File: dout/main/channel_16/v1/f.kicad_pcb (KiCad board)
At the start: 2 copper layers, 76.8 x 81.3 mm, 25 parts, among them J1 fm16_i, J10 dio_channel_i, J11 dio_channel_i, J12 dio_channel_i, J13 dio_channel_i, J14 dio_channel_i, J15 dio_channel_i, J16 dio_channel_i, J17 dio_channel_i, J18 data_manager_i, J19 data_manager_i, J2 dio_channel_i, J20 wrs_i, J21 wrs_i, J22 S0, J23 S1, J24 bus_i, J25 selector4_i, J3 dio_channel_i, J4 dio_channel_i, J5 dio_channel_i, J6 dio_channel_i, J7 dio_channel_i, J8 dio_channel_i, J9 dio_channel_i

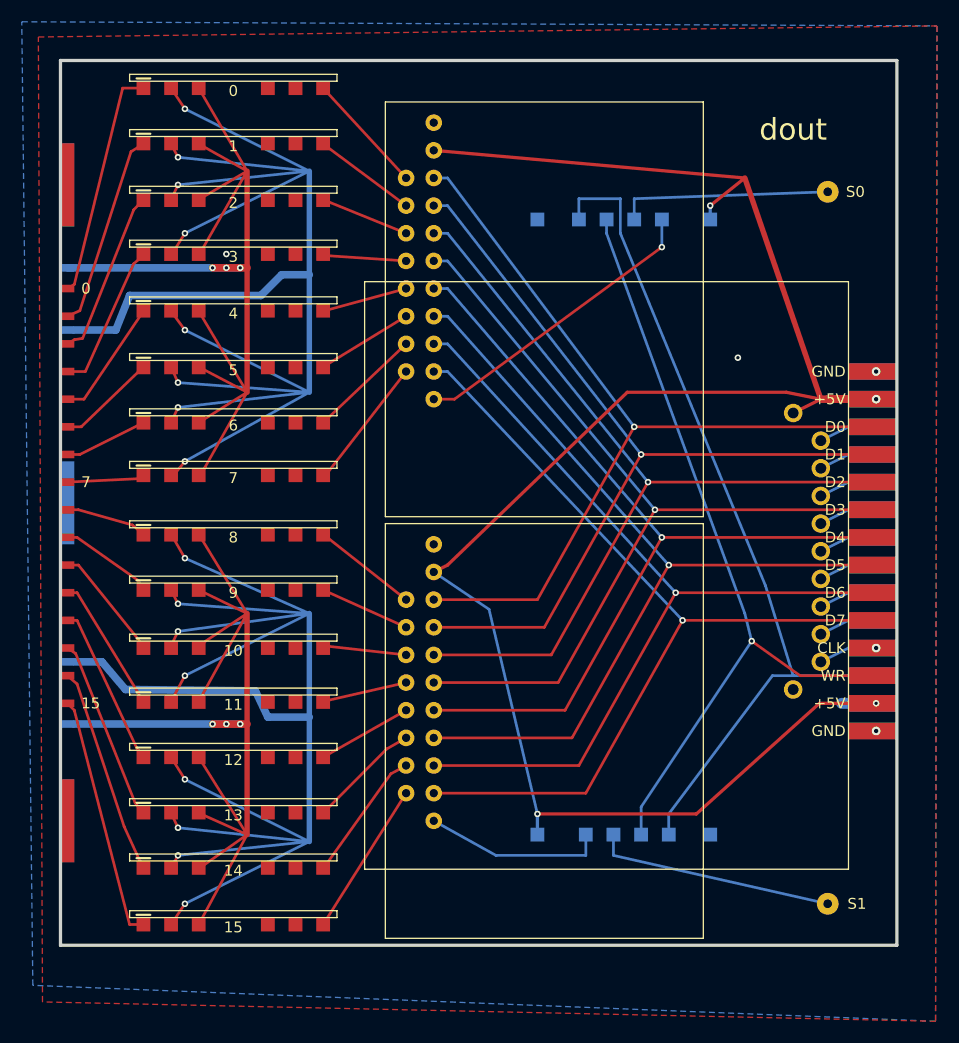
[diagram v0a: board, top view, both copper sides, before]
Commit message: voltage regulator for each module
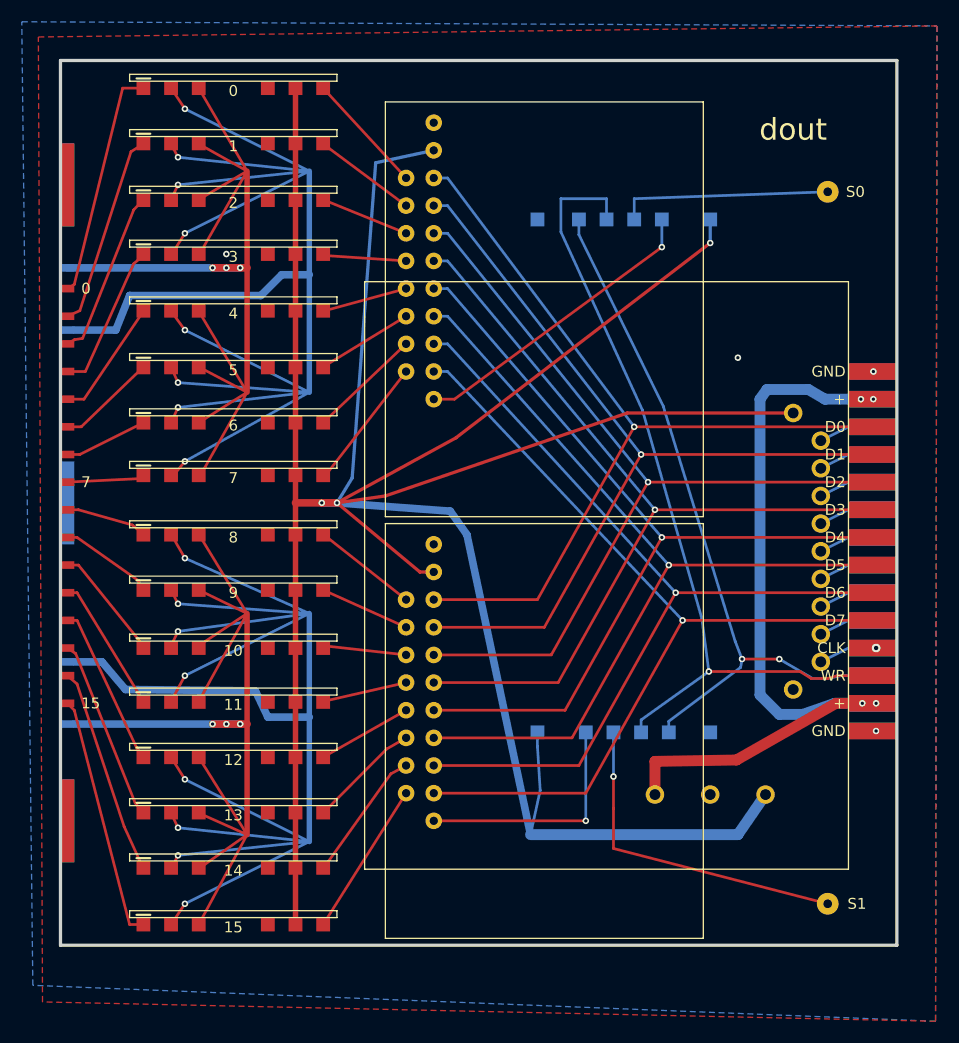
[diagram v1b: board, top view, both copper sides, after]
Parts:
- added J26: power_+5V, plc88:power_i, B.Cu at (3.81, 71.2)
- moved J21 9.40 mm to (8.26, 52.8)
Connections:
- J24 pad 25: +5V -> VPBUS
- J24 pad 26: +5V -> VPBUS
- J24 pad 3: +5V -> VPBUS
- J24 pad 4: +5V -> VPBUS
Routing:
- net +5V: track 175.1 -> 292.0 mm, vias 4 -> 3
- net VPBUS: track 0.00 -> 74.1 mm, vias 0 -> 4
- net RD: track 79.9 -> 65.9 mm, vias 0 -> 2
- net S1: track 22.1 -> 31.0 mm, vias 0 -> 1
- net SW1: track 16.7 -> 22.1 mm, vias 0 -> 1
- net WR: track 74.4 -> 76.1 mm
